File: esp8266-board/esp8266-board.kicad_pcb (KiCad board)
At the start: 2 copper layers, 15 parts, among them J1 StepDown-3A, J2 Barrel_Jack, J3 USB, J4 LED, J5 PGM, U1 ESP-12E

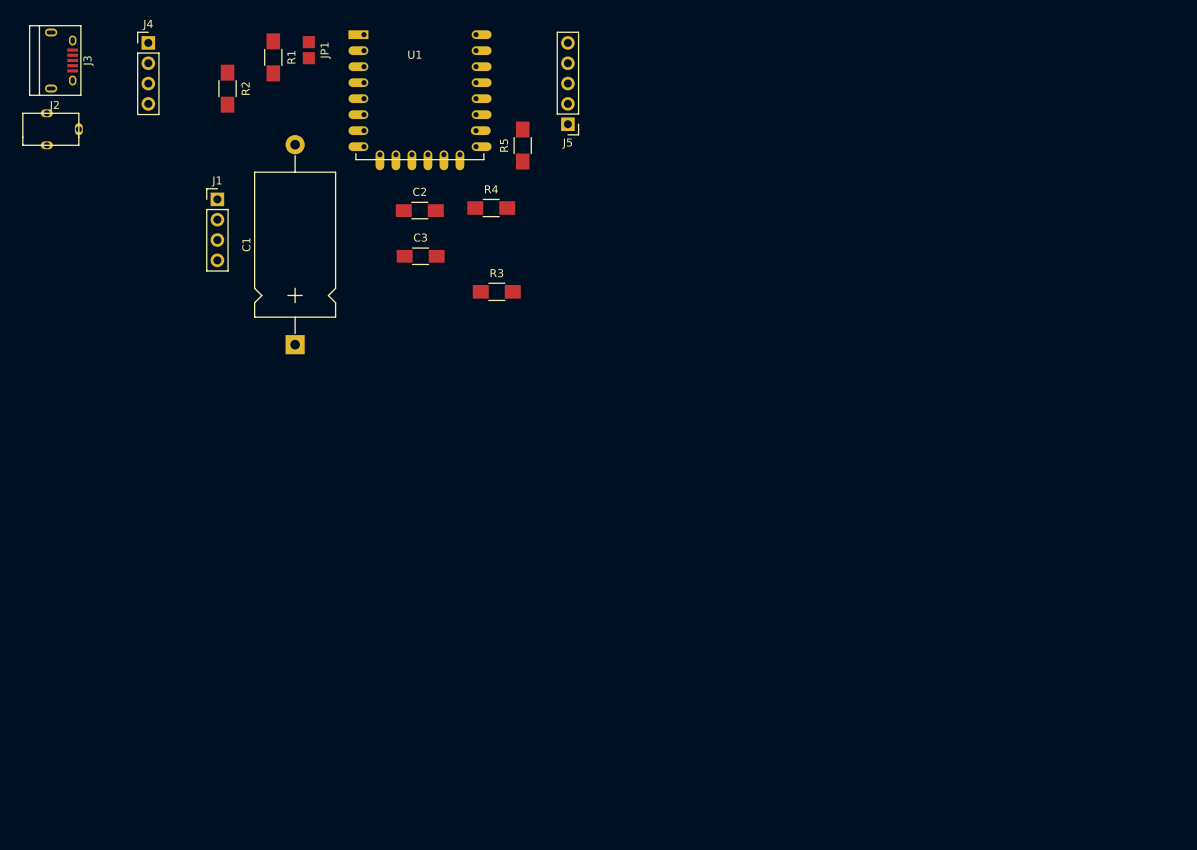
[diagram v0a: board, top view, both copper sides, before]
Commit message: Reogranizing and making use of new footprints
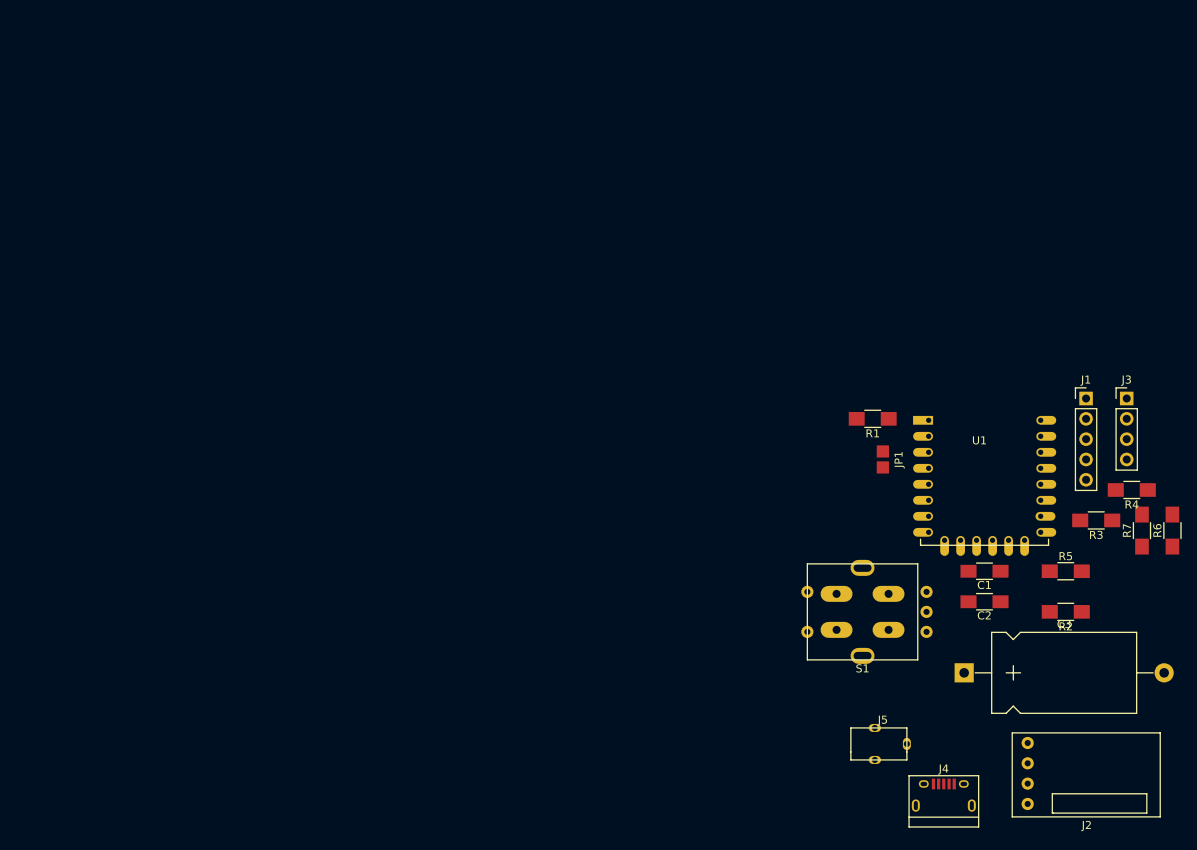
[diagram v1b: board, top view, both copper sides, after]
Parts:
- added R6: 1k, Resistors_SMD:R_1206_HandSoldering, F.Cu at (249.6, 125.7)
- added R7: 1k, Resistors_SMD:R_1206_HandSoldering, F.Cu at (245.7, 125.7)
- added S1: ROTARY_ENCODER_W_SPST, Switches:Rotary_Encoder_Or_Switch, F.Cu at (210.8, 135.9)
- C1: value 330uF -> 0.1uF; footprint Capacitors_THT:CP_Axial_L18.0mm_D10.0mm_P25.00mm_Horizontal -> Capacitors_SMD:C_1206_HandSoldering
- C2: value 0.1uF -> 1uF
- C3: value 1uF -> 330uF; footprint Capacitors_SMD:C_1206_HandSoldering -> Capacitors_THT:CP_Axial_L18.0mm_D10.0mm_P25.00mm_Horizontal
- J1: value StepDown-3A -> PGM; footprint Pin_Headers:Pin_Header_Straight_1x04_Pitch2.54mm -> Pin_Headers:Pin_Header_Straight_1x05_Pitch2.54mm
- J2: value Barrel_Jack -> StepDown-3A; footprint libraries:5.5mm_Barrel_Jack -> Voltage Regulators:SwitchingRegulator_Selectable
- J3: value USB -> LED; footprint Connectors:USB_Micro-B -> Pin_Headers:Pin_Header_Straight_1x04_Pitch2.54mm
- J4: value LED -> USB; footprint Pin_Headers:Pin_Header_Straight_1x04_Pitch2.54mm -> Connectors:USB_Micro-B
- J5: value PGM -> Barrel_Jack; footprint Pin_Headers:Pin_Header_Straight_1x05_Pitch2.54mm -> Power:5.5mm_Barrel_Jack
- JP1: footprint libraries:SolderJumper -> Features:SolderJumper
- moved J2 152.1 mm to (238.8, 156.2), turned to 0 degrees
- moved J3 139.9 mm to (243.8, 109.2), turned to 0 degrees
- moved J4 136.8 mm to (221.0, 158.8)
- moved R2 123.5 mm to (236.2, 135.9), turned to 180 degrees
- moved J1 111.4 mm to (238.8, 109.2)
- moved C1 90.7 mm to (226.1, 130.8), turned to 180 degrees
- moved JP1 88.1 mm to (213.4, 116.8)
- moved R1 87.5 mm to (212.1, 111.8), turned to 180 degrees
- moved R4 87.5 mm to (244.5, 120.7), turned to 180 degrees
- moved J5 86.9 mm to (213.4, 152.4)
- moved R5 86.3 mm to (236.2, 130.8), turned to 0 degrees
- moved C2 85.9 mm to (226.1, 134.6), turned to 180 degrees
- moved C3 85.6 mm to (223.5, 143.5)
- moved U1 85.5 mm to (219.1, 111.9)
- moved R3 80.2 mm to (240.0, 124.5), turned to 180 degrees
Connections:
- C1 pad 1: +3V3 -> GND
- C1 pad 2: GND -> +3V3
- C3 pad 1: GND -> +3V3
- C3 pad 2: +3V3 -> GND
- J1 pad 1: Net-(J1-Pad1) -> GND
- J1 pad 2: +5V -> TX
- J1 pad 3: GND -> RX
- J1 pad 4: +3V3 -> ~RST
- J2 pad 1: +5V -> Net-(J2-Pad1)
- J2 pad 2: GND -> +5V
- J2 pad 3: Net-(J2-Pad3) -> GND
- J3 pad 2: Net-(J3-Pad2) -> GND
- J3 pad 3: Net-(J3-Pad3) -> GPIO4
- J3 pad 4: Net-(J3-Pad4) -> GPIO5
- J4 pad 2: GND -> Net-(J4-Pad2)
- J4 pad 3: GPIO4 -> Net-(J4-Pad3)
- J4 pad 4: GPIO5 -> Net-(J4-Pad4)
- J5 pad 1: GND -> +5V
- J5 pad 2: ~FLASH -> GND
- J5 pad 3: ~RST -> Net-(J5-Pad3)
- R3 pad 1: +3V3 -> GND
- R3 pad 2: ~FLASH -> Net-(R3-Pad2)
- R4 pad 2: Net-(R4-Pad2) -> ~FLASH
- R5 pad 1: GND -> +3V3
- U1 pad 10: Net-(R5-Pad2) -> Net-(R3-Pad2)
- U1 pad 11: Net-(R4-Pad2) -> Net-(R5-Pad2)

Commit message: New voltage regulation structure in process
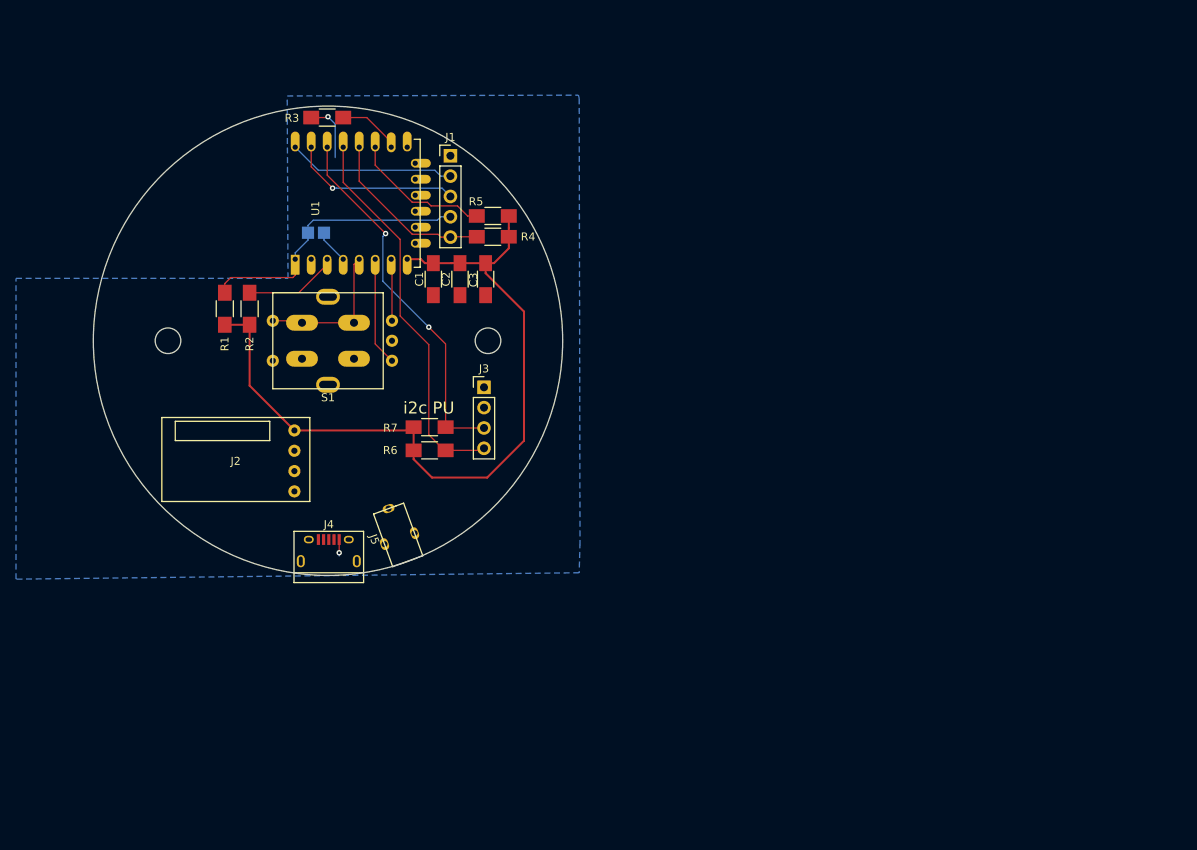
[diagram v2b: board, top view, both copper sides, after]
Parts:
- added REF**: MountingHole_3.2mm_M3, Mounting_Holes:MountingHole_3.2mm_M3, F.Cu at (124.0, 102.0)
- added REF**: MountingHole_3.2mm_M3, Mounting_Holes:MountingHole_3.2mm_M3, F.Cu at (164.0, 102.0)
- C2: value 1uF -> 10uF
- C3: value 330uF -> 2.2 uF; footprint Capacitors_THT:CP_Axial_L18.0mm_D10.0mm_P25.00mm_Horizontal -> Capacitors_SMD:C_1206_HandSoldering
- JP1: moved to B.Cu
- moved J2 113.3 mm to (132.5, 116.9), turned to 180 degrees
- moved R2 108.8 mm to (134.2, 98.0), turned to 270 degrees
- moved R3 108.5 mm to (143.9, 74.1), turned to 0 degrees
- moved R6 93.4 mm to (156.7, 115.7), turned to 0 degrees
- moved R7 90.0 mm to (156.7, 112.8), turned to 0 degrees
- moved R4 85.9 mm to (164.6, 89.0)
- moved J1 85.1 mm to (159.3, 78.9)
- moved R5 84.3 mm to (164.6, 86.4), turned to 180 degrees
- moved J4 82.7 mm to (144.1, 128.2)
- moved R1 82.2 mm to (131.1, 98.0), turned to 270 degrees
- moved U1 81.7 mm to (139.9, 91.8), turned to 90 degrees
- moved J3 80.4 mm to (163.5, 107.8)
- moved C1 78.0 mm to (157.2, 94.3), turned to 90 degrees
- moved C3 77.5 mm to (163.7, 94.3), turned to 270 degrees
- moved C2 77.0 mm to (160.5, 94.3), turned to 90 degrees
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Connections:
- J3 pad 3: GPIO4 -> GPIO5
- J3 pad 4: GPIO5 -> GPIO4
- S1 pad 1: GPIO12 -> GPIO14
- S1 pad 3: GPIO13 -> GPIO12
- S1 pad 5: GPIO14 -> GPIO13
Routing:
- net +3V3: track 0.00 -> 96.3 mm
- net GPIO4: track 0.00 -> 48.2 mm
- net GPIO5: track 0.00 -> 46.3 mm, vias 0 -> 2
- net ~RST: track 0.00 -> 35.5 mm
- net ~FLASH: track 0.00 -> 21.9 mm
- net RX: track 0.00 -> 21.4 mm, vias 0 -> 1
- net TX: track 0.00 -> 20.9 mm
- net GPIO14: track 0.00 -> 19.1 mm
- net Net-(R5-Pad2): track 0.00 -> 17.6 mm
- net GPIO12: track 0.00 -> 13.6 mm
- net Net-(R2-Pad1): track 0.00 -> 11.8 mm
- net GND: track 0.00 -> 9.66 mm, vias 0 -> 2
- net Net-(R3-Pad2): track 0.00 -> 7.91 mm
- net GPIO13: track 0.00 -> 7.74 mm
- net GPIO16: track 0.00 -> 4.30 mm
- added copper zone on B.Cu, net GND
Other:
- board outline added: 58.7 x 58.7 mm
- net class 3.3V PWR added: clearance 0.254, trace_width 0.254, via_dia 0.6858, via_drill 0.3302
- net class 5V PWR: clearance 0.3 -> 0.762; trace_width 0.5 -> 0.762; via_dia 0.6 -> 0.6858; via_drill 0.4 -> 0.3302
- net class Default: clearance 0.2 -> 0.254; trace_width 0.25 -> 0.1524; via_dia 0.6 -> 0.6858; via_drill 0.4 -> 0.3302
- rule trace_clearance: 0.2 -> 0.254
- rule trace_min: 0.2 -> 0.1524
- rule via_min_drill: 0.3 -> 0.3302
- rule via_min_size: 0.4 -> 0.6858
- board text added: "i2c PU"

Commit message: First board rev order 0.1
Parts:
- removed the REF** at (164.0, 102.0)
- added C4: 10uF, Capacitors_SMD:C_1206_HandSoldering, F.Cu at (145.7, 114.9)
- added C5: 300uF, Capacitors_THT:CP_Radial_D8.0mm_P5.00mm, F.Cu at (134.0, 106.4)
- added JP2: 3.3V, Features:SolderJumper, F.Cu at (163.6, 100.8)
- added JP3: 5V, Features:SolderJumper, F.Cu at (163.6, 103.2)
- added R8: 10k, Resistors_SMD:R_1206_HandSoldering, F.Cu at (151.4, 111.6)
- added U2: AP2112, TO_SOT_Packages_SMD:SOT-23-5, F.Cu at (145.5, 111.9)
- added U3: AMS1117-3.3, TO_SOT_Packages_SMD:SOT-223, F.Cu at (132.5, 120.4)
- J4: footprint Connectors:USB_Micro-B -> Power:USB_Micro-B
- R6, R7: footprint Resistors_SMD:R_1206_HandSoldering -> Resistors_SMD:R_0805_HandSoldering
- moved R6 1.68 mm to (158.4, 115.6)
- moved R7 1.65 mm to (158.3, 112.9)
- moved J5 1.16 mm to (152.8, 124.7)
- moved J1 0.51 mm to (159.3, 79.4)
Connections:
- J2 pad 1: Net-(J2-Pad1) -> (no net)
- J3 pad 1: +5V -> Net-(J3-Pad1)
- J4 pad 2: Net-(J4-Pad2) -> (no net)
- J4 pad 3: Net-(J4-Pad3) -> (no net)
- J4 pad 4: Net-(J4-Pad4) -> (no net)
- J5 pad 3: Net-(J5-Pad3) -> GND
- U1 pad 17: Net-(U1-Pad17) -> (no net)
- U1 pad 18: Net-(U1-Pad18) -> (no net)
- U1 pad 19: Net-(U1-Pad19) -> (no net)
- U1 pad 2: ADC -> (no net)
- U1 pad 20: Net-(U1-Pad20) -> (no net)
- U1 pad 21: Net-(U1-Pad21) -> (no net)
- U1 pad 22: Net-(U1-Pad22) -> (no net)
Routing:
- net +5V: track 0.00 -> 64.8 mm, vias 0 -> 1
- net GND: track 9.66 -> 31.1 mm, vias 2 -> 6
- net Net-(J3-Pad1): track 0.00 -> 9.37 mm
- net +3V3: track 96.3 -> 105.4 mm, vias 0 -> 2
- net Net-(R8-Pad2): track 0.00 -> 3.92 mm
- net Net-(R3-Pad2): track 7.91 -> 8.48 mm
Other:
- board size 58.7 x 58.7 mm -> 59.4 x 59.4 mm
- net class 5V PWR: clearance 0.762 -> 0.254; trace_width 0.762 -> 0.5
- board text added: "3.3V OR 5V"
- board text added: "5v In"
- board text added: "AMS1117"
- board text added: "AP2112"
- board text added: "ESP8266 Puck Rev v0.1"
- board text added: "Pop Only One 3.3V Reg"
- board text added: "i2c"
- board text removed: "i2c PU"
